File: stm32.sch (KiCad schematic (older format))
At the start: 29 parts, among them J6 USB_C_Receptacle_USB2.0, U3 STM32F205RBTx, U4 OLED_0.96\"_SSD1306, Y2 8M

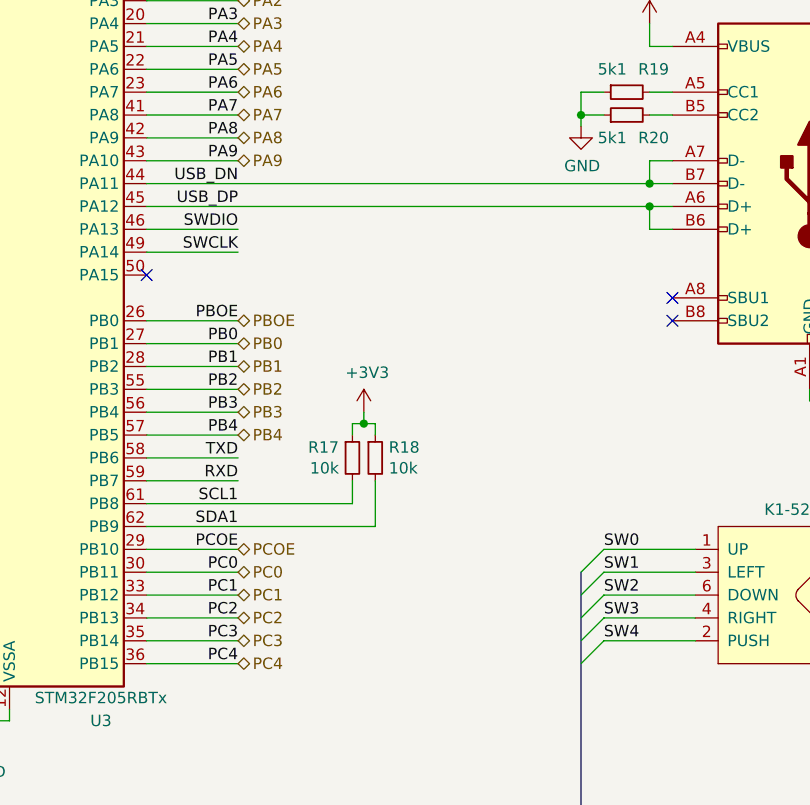
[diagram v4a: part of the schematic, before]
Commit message: Routing should be done
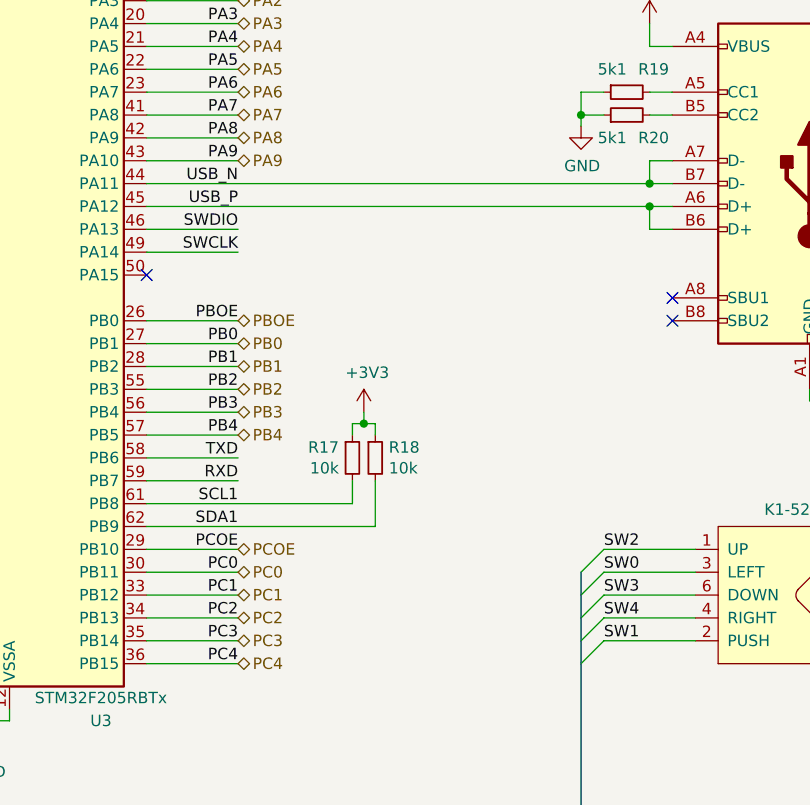
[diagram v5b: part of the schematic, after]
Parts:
- J6: footprint Connector_USB:USB_C_Receptacle_Palconn_UTC16-G -> antboard:USB_C_Receptacle_Palconn_UTC16-G
- Y2: footprint Crystal:Crystal_HC18-U_Vertical -> Crystal:Crystal_HC49-4H_Vertical
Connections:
- net SW0: now also S1.3 (LEFT); no longer S1.1 (UP)
- net SW1: now also S1.2 (PUSH); no longer S1.3 (LEFT)
- net SW2: now also S1.1 (UP); no longer S1.6 (DOWN)
- net SW3: now also S1.6 (DOWN); no longer S1.4 (RIGHT)
- net SW4: now also S1.4 (RIGHT); no longer S1.2 (PUSH)
- net USB_DN renamed USB_N
- net USB_DP renamed USB_P
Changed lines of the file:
@@
 F 0 "Y2" H 3800 4218 50  0000 C CNN
 F 1 "8M" H 3800 4127 50  0000 C CNN
-F 2 "Crystal:Crystal_HC18-U_Vertical" H 3800 3950 50  0001 C CNN
+F 2 "Crystal:Crystal_HC49-4H_Vertical" H 3800 3950 50  0001 C CNN
 F 3 "~" H 3800 3950 50  0001 C CNN
 	1    3800 3950
@@
 F 0 "J6" H 8870 3489 50  0000 R CNN
 F 1 "USB_C_Receptacle_USB2.0" H 8870 3398 50  0000 R CNN
-F 2 "Connector_USB:USB_C_Receptacle_Palconn_UTC16-G" H 9450 3550 50  0001 C CNN
+F 2 "antboard:USB_C_Receptacle_Palconn_UTC16-G" H 9450 3550 50  0001 C CNN
 F 3 "https://www.usb.org/sites/default/files/documents/usb_type-c.zip" H 9450 3550 50  0001 C CNN
 	1    9300 3550
@@
 $EndComp
 Text Label 6800 3550 2    50   ~ 0
-USB_DN
+USB_N
 Text Label 6800 3650 2    50   ~ 0
-USB_DP
+USB_P
 Wire Wire Line
 	6400 3550 8600 3550
@@
 Entry Wire Line
 	8300 5250 8400 5150
-Text Label 8400 5550 0    50   ~ 0
+Text Label 8400 5450 0    50   ~ 0
 SW4
-Wire Wire Line
-	8800 5550 8400 5550
-Text Label 8400 5450 0    50   ~ 0
-SW3
 Wire Wire Line
 	8800 5450 8400 5450
 Text Label 8400 5350 0    50   ~ 0
+SW3
+Wire Wire Line
+	8800 5350 8400 5350
+Text Label 8400 5150 0    50   ~ 0
 SW2
 Wire Wire Line
-	8800 5350 8400 5350
+	8800 5150 8400 5150
+Text Label 8400 5550 0    50   ~ 0
+SW1
+Wire Wire Line
+	8800 5550 8400 5550
 Text Label 8400 5250 0    50   ~ 0
-SW1
+SW0
 Wire Wire Line
 	8800 5250 8400 5250
-Text Label 8400 5150 0    50   ~ 0
-SW0
-Wire Wire Line
-	8800 5150 8400 5150
 Wire Wire Line
 	10000 5350 10000 5450

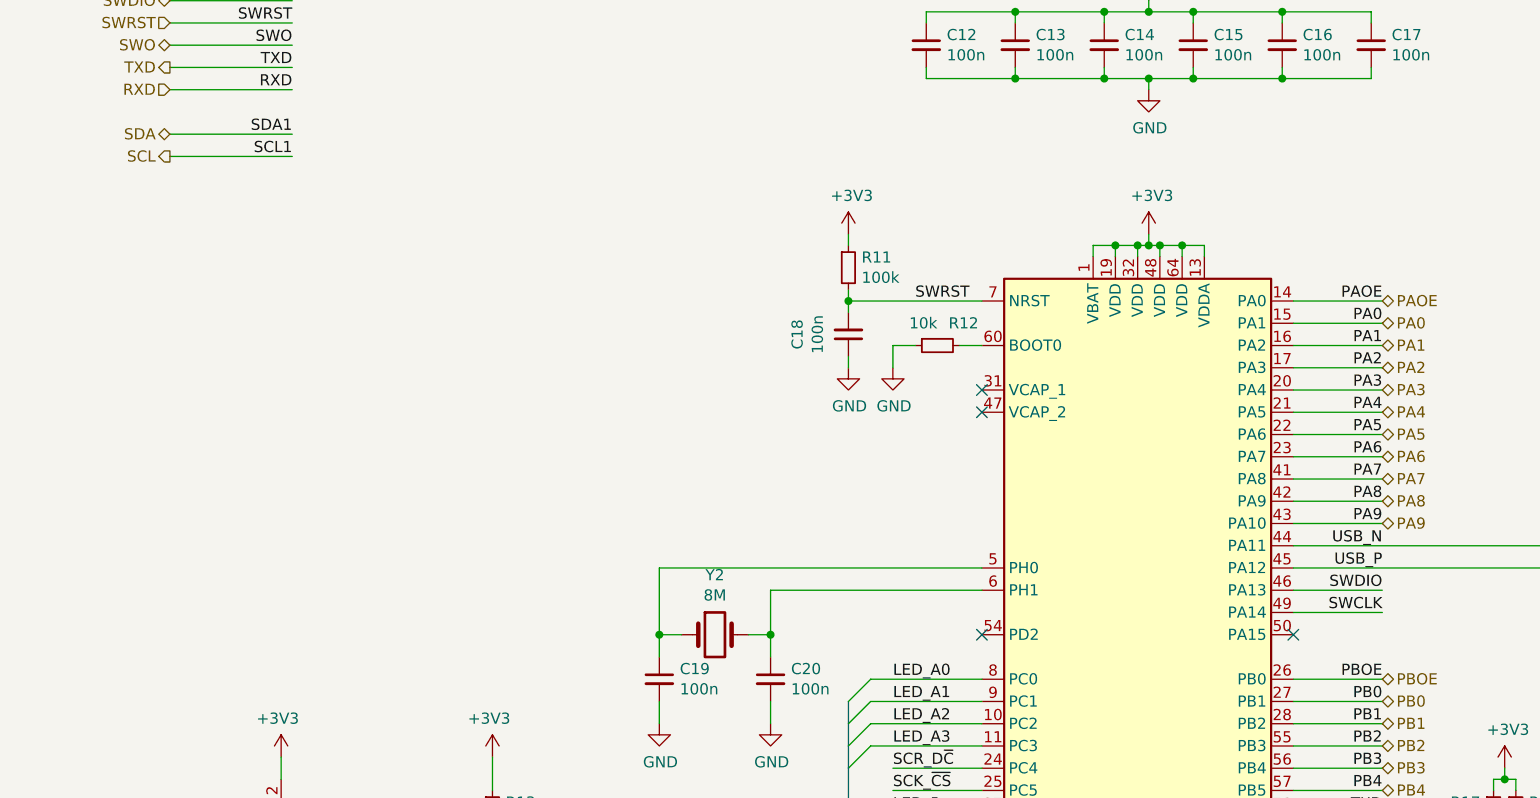
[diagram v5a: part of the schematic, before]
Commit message: sch, pcb: Add ADC to read set IO voltages
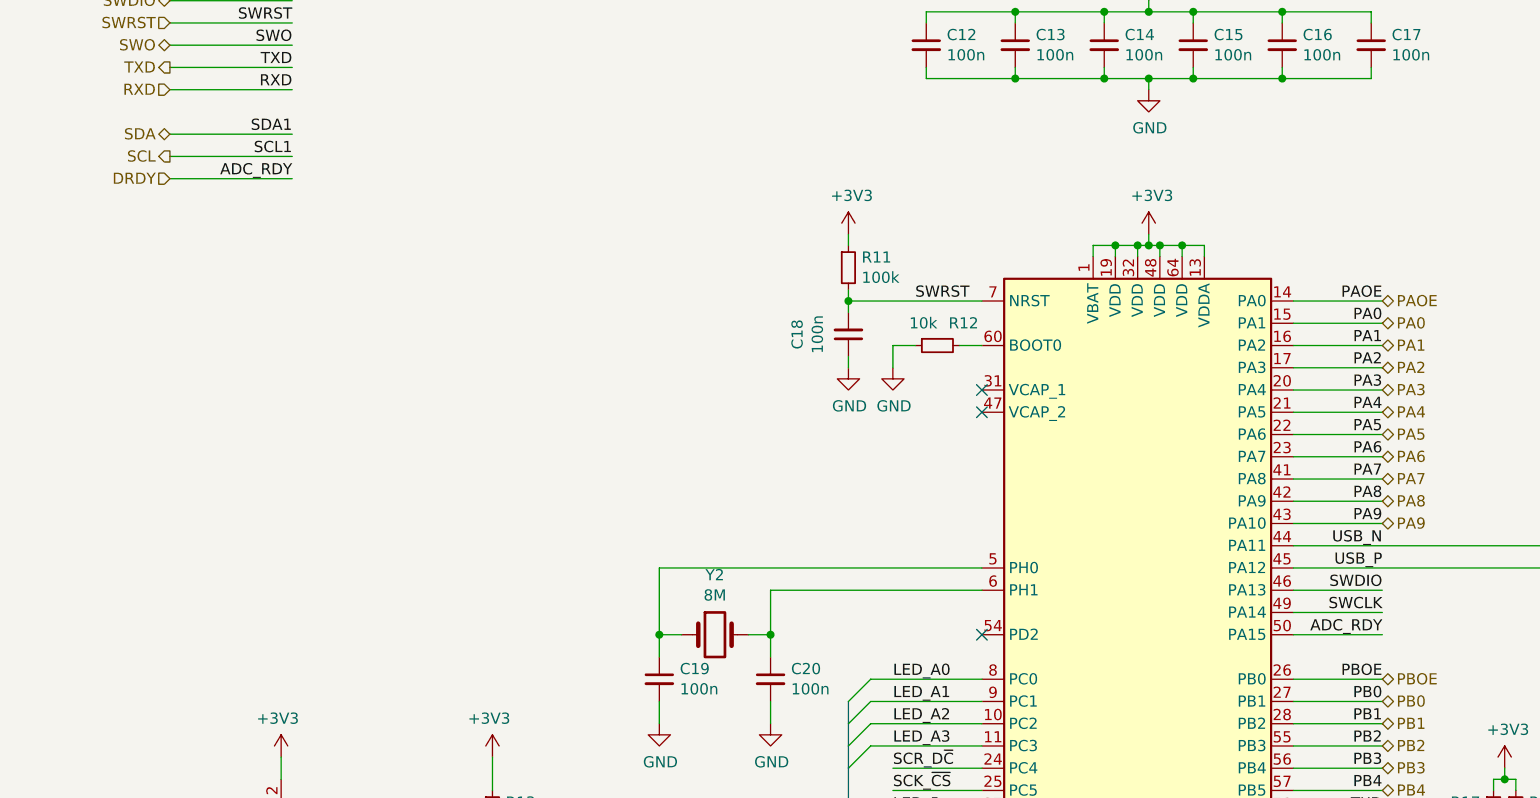
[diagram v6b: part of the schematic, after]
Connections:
- net DRDY: now reaches U3.50 (PA15)
- no-connect marks 6 -> 5
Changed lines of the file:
@@
 NoConn ~ 5000 2850
 NoConn ~ 5000 2950
-NoConn ~ 6400 3950
 $Comp
 L Connector:USB_C_Receptacle_USB2.0 J6
@@
 	1850 5400 1850 5500
 NoConn ~ 5000 3950
+Wire Wire Line
+	1350 1900 1900 1900
+Text Label 1900 1900 2    50   ~ 0
+ADC_RDY
+Text HLabel 1350 1900 0    50   Input ~ 0
+DRDY
+Wire Wire Line
+	6400 3950 6800 3950
+Text Label 6800 3950 2    50   ~ 0
+ADC_RDY
 Wire Bus Line
 	4400 4250 4400 6450

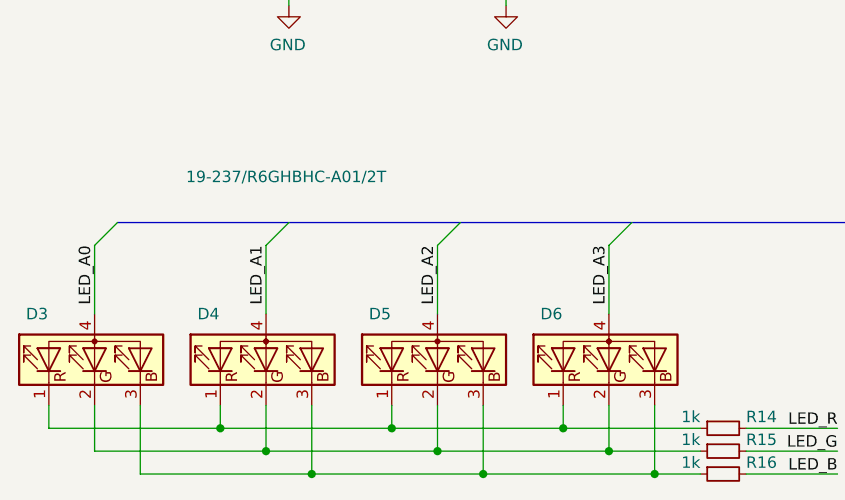
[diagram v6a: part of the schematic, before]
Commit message: sch, pcb: Change RGB LEDs to MHPA1515
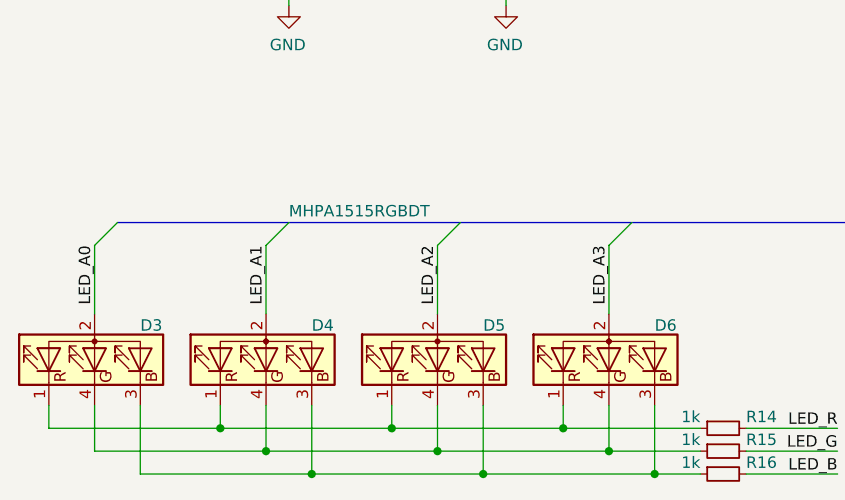
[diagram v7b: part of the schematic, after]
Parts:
- removed D3, D4, D5, D6: 19-237/R6GHBHC-A01/2T, antboard:19-237_R6GHBHC-A01_2T, symbol Device:LED_RGBA
- added D3, D4, D5, D6: MHPA1515RGBDT, antboard:PLCC1515, symbol Device:LED_RABG
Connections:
- net LED_A0: now also D3.2 (A)
- net LED_A1: now also D4.2 (A)
- net LED_A2: now also D5.2 (A)
- net LED_A3: now also D6.2 (A)
- net at R14.1: now also D3.1 (RK), D4.1 (RK), D5.1 (RK), D6.1 (RK)
- net at R15.1: now also D3.4 (GK), D4.4 (GK), D5.4 (GK), D6.4 (GK)
- net at R16.1: now also D3.3 (BK), D4.3 (BK), D5.3 (BK), D6.3 (BK)
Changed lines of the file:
@@
 Text Label 4600 4450 0    50   ~ 0
 LED_A3
-$Comp
-L Device:LED_RGBA D6
-U 1 1 5E06E532
-P 3250 7050
-F 0 "D6" V 3450 7350 50  0000 R CNN
-F 1 "19-237/R6GHBHC-A01/2T" V 4050 6650 50  0001 R CNN
-F 2 "antboard:19-237_R6GHBHC-A01_2T" H 3250 7000 50  0001 C CNN
-F 3 "~" H 3250 7000 50  0001 C CNN
-	1    3250 7050
-	0    -1   -1   0
-$EndComp
-$Comp
-L Device:LED_RGBA D5
-U 1 1 5E06D7A2
-P 2500 7050
-F 0 "D5" V 2700 7350 50  0000 R CNN
-F 1 "19-237/R6GHBHC-A01/2T" V 3300 6650 50  0001 R CNN
-F 2 "antboard:19-237_R6GHBHC-A01_2T" H 2500 7000 50  0001 C CNN
-F 3 "~" H 2500 7000 50  0001 C CNN
-	1    2500 7050
-	0    -1   -1   0
-$EndComp
-$Comp
-L Device:LED_RGBA D4
-U 1 1 5E06BB7B
-P 1750 7050
-F 0 "D4" V 1950 7350 50  0000 R CNN
-F 1 "19-237/R6GHBHC-A01/2T" V 2550 6650 50  0001 R CNN
-F 2 "antboard:19-237_R6GHBHC-A01_2T" H 1750 7000 50  0001 C CNN
-F 3 "~" H 1750 7000 50  0001 C CNN
-	1    1750 7050
-	0    -1   -1   0
-$EndComp
 Connection ~ 2700 7550
 Connection ~ 1950 7550
@@
 Wire Wire Line
 	1000 6850 1000 6550
-$Comp
-L Device:LED_RGBA D3
-U 1 1 5DF6533B
-P 1000 7050
-F 0 "D3" V 1200 7350 50  0000 R CNN
-F 1 "19-237/R6GHBHC-A01/2T" V 1800 6650 50  0000 R CNN
-F 2 "antboard:19-237_R6GHBHC-A01_2T" H 1000 7000 50  0001 C CNN
-F 3 "~" H 1000 7000 50  0001 C CNN
-	1    1000 7050
-	0    -1   -1   0
-$EndComp
 Wire Bus Line
 	4500 6450 8300 6450
@@
 Wire Bus Line
 	8300 5250 8300 6450
+$Comp
+L Device:LED_RABG D3
+U 1 1 5E2C9CFE
+P 1000 7050
+F 0 "D3" V 1150 6850 50  0000 R CNN
+F 1 "MHPA1515RGBDT" V 1650 6200 50  0000 R CNN
+F 2 "antboard:PLCC1515" H 1000 7000 50  0001 C CNN
+F 3 "~" H 1000 7000 50  0001 C CNN
+	1    1000 7050
+	0    -1   -1   0
+$EndComp
+$Comp
+L Device:LED_RABG D4
+U 1 1 5E2D0755
+P 1750 7050
+F 0 "D4" V 1900 6850 50  0000 R CNN
+F 1 "MHPA1515RGBDT" V 1705 6720 50  0001 R CNN
+F 2 "antboard:PLCC1515" H 1750 7000 50  0001 C CNN
+F 3 "~" H 1750 7000 50  0001 C CNN
+	1    1750 7050
+	0    -1   -1   0
+$EndComp
+$Comp
+L Device:LED_RABG D5
+U 1 1 5E2D1265
+P 2500 7050
+F 0 "D5" V 2650 6850 50  0000 R CNN
+F 1 "MHPA1515RGBDT" V 2455 6720 50  0001 R CNN
+F 2 "antboard:PLCC1515" H 2500 7000 50  0001 C CNN
+F 3 "~" H 2500 7000 50  0001 C CNN
+	1    2500 7050
+	0    -1   -1   0
+$EndComp
+$Comp
+L Device:LED_RABG D6
+U 1 1 5E2D1CE0
+P 3250 7050
+F 0 "D6" V 3400 6850 50  0000 R CNN
+F 1 "MHPA1515RGBDT" V 3205 6720 50  0001 R CNN
+F 2 "antboard:PLCC1515" H 3250 7000 50  0001 C CNN
+F 3 "~" H 3250 7000 50  0001 C CNN
+	1    3250 7050
+	0    -1   -1   0
+$EndComp
 $EndSCHEMATC
